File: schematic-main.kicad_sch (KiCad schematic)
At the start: 12 parts, among them J1 Fell_Cell_Conn_01x02_Pin, J2 Conn_01x02, J3 Conn_01x02, J4 Conn_01x03, J5 Conn_01x02, J6 Conn_01x03, J7 Conn_01x02, P1 USB_C_Plug_USB2.0

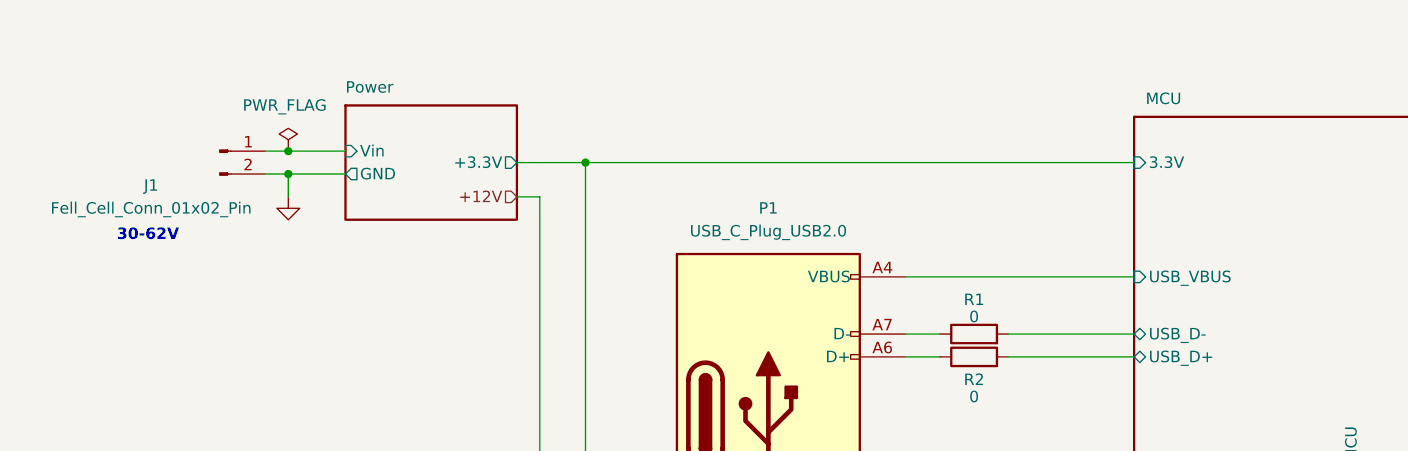
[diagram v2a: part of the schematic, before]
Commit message: Add Schottky Diode for VBUS and Vreg
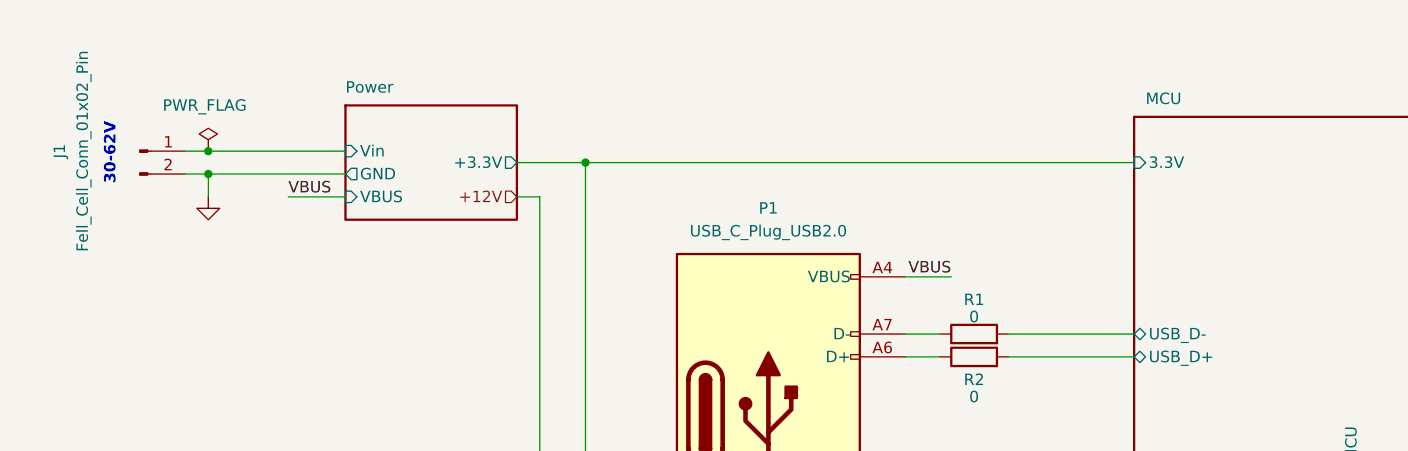
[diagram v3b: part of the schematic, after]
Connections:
- net MCU/USB_VBUS renamed VBUS
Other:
- sheet MCU ports: added none; removed USB_VBUS
- sheet Power  ports: added VBUS; removed none
- moved on the sheet: J1
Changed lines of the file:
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@@
     (company "Hydrogreen Pollub")
   )
-  (junction (at 40.64 34.29) (diameter 0) (color 0 0 0 0)
+  (junction (at 31.75 34.29) (diameter 0) (color 0 0 0 0)
   )
   (junction (at 102.87 85.09) (diameter 0) (color 0 0 0 0)
@@
   (junction (at 93.98 85.09) (diameter 0) (color 0 0 0 0)
   )
-  (junction (at 40.64 31.75) (diameter 0) (color 0 0 0 0)
+  (junction (at 31.75 31.75) (diameter 0) (color 0 0 0 0)
   )
   (junction (at 73.66 33.02) (diameter 0) (color 0 0 0 0)
@@
     (stroke (width 0) (type default))
   )
-  (wire (pts (xy 38.1 31.75) (xy 40.64 31.75))
+  (wire (pts (xy 29.21 31.75) (xy 31.75 31.75))
     (stroke (width 0) (type default))
   )
@@
     (stroke (width 0) (type default))
   )
-  (wire (pts (xy 40.64 34.29) (xy 46.99 34.29))
+  (wire (pts (xy 31.75 34.29) (xy 46.99 34.29))
     (stroke (width 0) (type default))
   )
@@
     (stroke (width 0) (type default))
   )
-  (wire (pts (xy 109.22 45.72) (xy 134.62 45.72))
-    (stroke (width 0) (type default))
-  )
   (wire (pts (xy 118.11 85.09) (xy 118.11 83.82))
     (stroke (width 0) (type default))
@@
     (stroke (width 0) (type default))
   )
-  (wire (pts (xy 38.1 34.29) (xy 40.64 34.29))
+  (wire (pts (xy 29.21 34.29) (xy 31.75 34.29))
     (stroke (width 0) (type default))
   )
@@
     (stroke (width 0) (type default))
   )
+  (wire (pts (xy 40.64 36.83) (xy 46.99 36.83))
+    (stroke (width 0) (type default))
+  )
   (wire (pts (xy 179.07 123.19) (xy 189.23 123.19))
     (stroke (width 0) (type default))
@@
     (stroke (width 0) (type default))
   )
-  (wire (pts (xy 40.64 34.29) (xy 40.64 36.83))
+  (wire (pts (xy 31.75 34.29) (xy 31.75 36.83))
     (stroke (width 0) (type default))
   )
@@
     (stroke (width 0) (type default))
   )
-  (wire (pts (xy 40.64 31.75) (xy 46.99 31.75))
+  (wire (pts (xy 31.75 31.75) (xy 46.99 31.75))
+    (stroke (width 0) (type default))
+  )
+  (wire (pts (xy 114.3 45.72) (xy 109.22 45.72))
     (stroke (width 0) (type default))
   )
@@
     (stroke (width 0) (type default))
   )
-  (text "30-62V" (at 21.59 41.91 0)
+  (text "30-62V" (at 21.59 35.56 90)
     (effects (font (size 1.27 1.27) (thickness 0.254) bold) (justify left bottom))
+  )
+  (label "VBUS" (at 40.64 36.83 0) (fields_autoplaced)
+    (effects (font (size 1.27 1.27)) (justify left bottom))
+  )
+  (label "VBUS" (at 114.3 45.72 180) (fields_autoplaced)
+    (effects (font (size 1.27 1.27)) (justify right bottom))
   )
   (hierarchical_label "out_12V" (shape input) (at 157.48 163.83 90) (fields_autoplaced)
@@
     )
   )
-  (symbol (lib_id "Connector:Conn_01x02_Pin") (at 33.02 31.75 0) (unit 1)
+  (symbol (lib_id "Connector:Conn_01x02_Pin") (at 24.13 31.75 0) (unit 1)
     (in_bom yes) (on_board yes) (dnp no)
-    (property "Reference" "J1" (at 25.4 35.56 0)
-      (effects (font (size 1.27 1.27)))
-    )
-    (property "Value" "Fell_Cell_Conn_01x02_Pin" (at 25.4 38.1 0)
-      (effects (font (size 1.27 1.27)))
-    )
-    (property "Footprint" "" (at 33.02 31.75 0)
-      (effects (font (size 1.27 1.27)) hide)
-    )
-    (property "Datasheet" "~" (at 33.02 31.75 0)
+    (property "Reference" "J1" (at 15.24 31.75 90)
+      (effects (font (size 1.27 1.27)))
+    )
+    (property "Value" "Fell_Cell_Conn_01x02_Pin" (at 17.78 31.75 90)
+      (effects (font (size 1.27 1.27)))
+    )
+    (property "Footprint" "" (at 24.13 31.75 0)
+      (effects (font (size 1.27 1.27)) hide)
+    )
+    (property "Datasheet" "~" (at 24.13 31.75 0)
       (effects (font (size 1.27 1.27)) hide)
     )
@@
     )
   )
-  (symbol (lib_id "power:GND") (at 40.64 36.83 0) (unit 1)
-    (in_bom yes) (on_board yes) (dnp no) (fields_autoplaced)
-    (property "Reference" "#PWR01" (at 40.64 43.18 0)
-      (effects (font (size 1.27 1.27)) hide)
-    )
-    (property "Value" "GND" (at 40.64 41.91 0)
-      (effects (font (size 1.27 1.27)) hide)
-    )
-    (property "Footprint" "" (at 40.64 36.83 0)
-      (effects (font (size 1.27 1.27)) hide)
-    )
-    (property "Datasheet" "" (at 40.64 36.83 0)
+  (symbol (lib_id "power:GND") (at 31.75 36.83 0) (unit 1)
+    (in_bom yes) (on_board yes) (dnp no) (fields_autoplaced)
+    (property "Reference" "#PWR01" (at 31.75 43.18 0)
+      (effects (font (size 1.27 1.27)) hide)
+    )
+    (property "Value" "GND" (at 31.75 41.91 0)
+      (effects (font (size 1.27 1.27)) hide)
+    )
+    (property "Footprint" "" (at 31.75 36.83 0)
+      (effects (font (size 1.27 1.27)) hide)
+    )
+    (property "Datasheet" "" (at 31.75 36.83 0)
       (effects (font (size 1.27 1.27)) hide)
     )
@@
     )
   )
-  (symbol (lib_id "power:PWR_FLAG") (at 40.64 31.75 0) (unit 1)
+  (symbol (lib_id "power:PWR_FLAG") (at 31.75 31.75 0) (unit 1)
     (in_bom yes) (on_board yes) (dnp no)
-    (property "Reference" "#FLG01" (at 40.64 29.845 0)
-      (effects (font (size 1.27 1.27)) hide)
-    )
-    (property "Value" "PWR_FLAG" (at 35.56 26.67 0)
-      (effects (font (size 1.27 1.27)) (justify left))
-    )
-    (property "Footprint" "" (at 40.64 31.75 0)
-      (effects (font (size 1.27 1.27)) hide)
-    )
-    (property "Datasheet" "~" (at 40.64 31.75 0)
+    (property "Reference" "#FLG01" (at 31.75 29.845 0)
+      (effects (font (size 1.27 1.27)) hide)
+    )
+    (property "Value" "PWR_FLAG" (at 26.67 26.67 0)
+      (effects (font (size 1.27 1.27)) (justify left))
+    )
+    (property "Footprint" "" (at 31.75 31.75 0)
+      (effects (font (size 1.27 1.27)) hide)
+    )
+    (property "Datasheet" "~" (at 31.75 31.75 0)
       (effects (font (size 1.27 1.27)) hide)
     )
@@
       (effects (font (size 1.27 1.27)) (justify left))
     )
+    (pin "VBUS" input (at 46.99 36.83 180)
+      (effects (font (size 1.27 1.27)) (justify left))
+    )
     (instances
       (project "schematic-main"
@@
       (effects (font (size 1.27 1.27)) (justify left))
     )
-    (pin "USB_VBUS" input (at 134.62 45.72 180)
-      (effects (font (size 1.27 1.27)) (justify left))
-    )

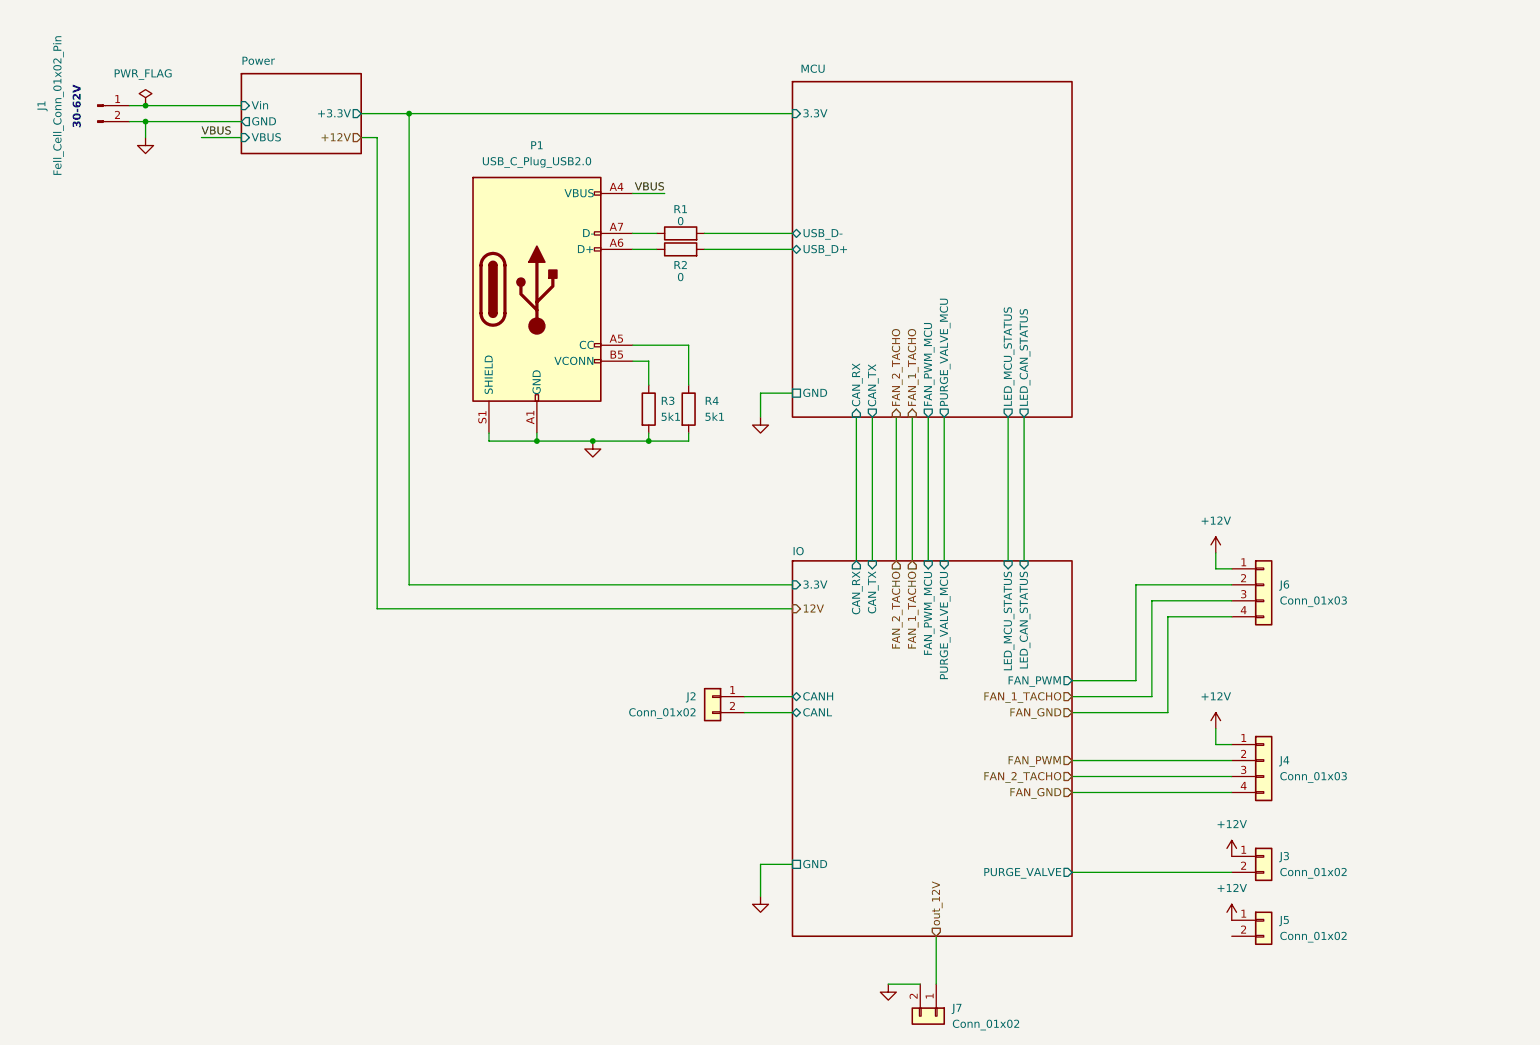
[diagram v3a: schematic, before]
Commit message: Add FC voltage measure, axilary input and output
Schematic complet?
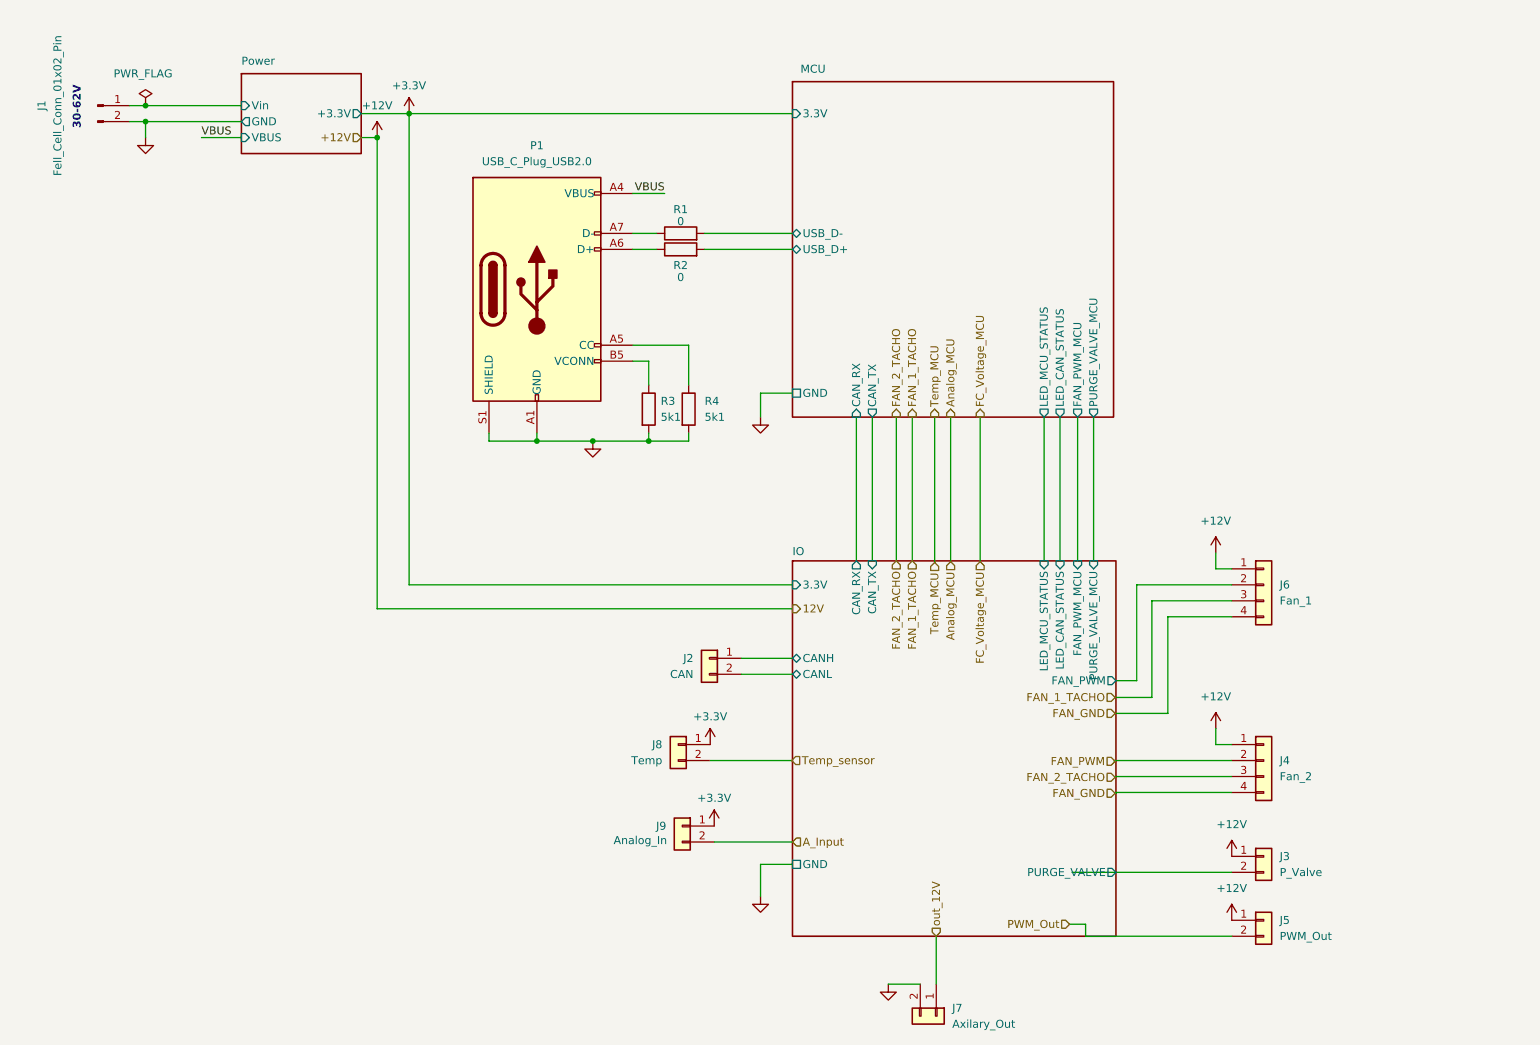
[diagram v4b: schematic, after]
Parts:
- added J8: Temp, symbol Connector_Generic:Conn_01x02
- added J9: Analog_In, symbol Connector_Generic:Conn_01x02
- J2: value Conn_01x02 -> CAN
- J3: value Conn_01x02 -> P_Valve
- J4: value Conn_01x03 -> Fan_2
- J5: value Conn_01x02 -> PWM_Out
- J6: value Conn_01x03 -> Fan_1
- J7: value Conn_01x02 -> Axilary_Out
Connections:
- net IO/PURGE_VALVE: no longer J3.2 (Pin_2)
- net PWM_Out: now reaches J5.2 (Pin_2)
- new net +3.3V: J8.1 (Pin_1), J9.1 (Pin_1)
- new net A_Input: J9.2 (Pin_2)
- new net Temp_sensor: J8.2 (Pin_2)
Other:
- title: Fuel cell control unit -> Fuel Cell Control Unit  (FCCU)
- moved on the sheet: J2
